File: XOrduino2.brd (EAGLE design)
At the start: 94 x 54.1 mm, 82 parts, among them J1 2.5mm, J2 2.5mm, J3 2.5mm, J4 2.5mm, J5 Batt In, J6 MOT R, J7 MOT L, P1 10k, Q1 ALS-PT204-6C/L177, SW1 RESET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

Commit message: v5 gerbers.
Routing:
- net GND: track 397.7 -> 416.2 mm, vias 6 -> 10
- net RD_P: track 26.5 -> 33.7 mm
- net +5V: track 226.1 -> 228.0 mm, vias 5 -> 7
- net XUSB: track 42.7 -> 44.4 mm
- net AREF: track 80.0 -> 81.5 mm
- net A2: track 44.5 -> 45.8 mm
- net A0: track 65.3 -> 64.3 mm
- net A1: track 57.2 -> 56.4 mm
- net N$8: track 99.0 -> 98.2 mm
- net MISO: track 30.2 -> 31.0 mm
- net N$11: track 26.1 -> 26.8 mm
- net VUSB: track 44.5 -> 43.9 mm
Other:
- board size 94 x 54.1 mm -> 81.3 x 53.3 mm
- board text added: "Alt Routing for LIGHT/A5"

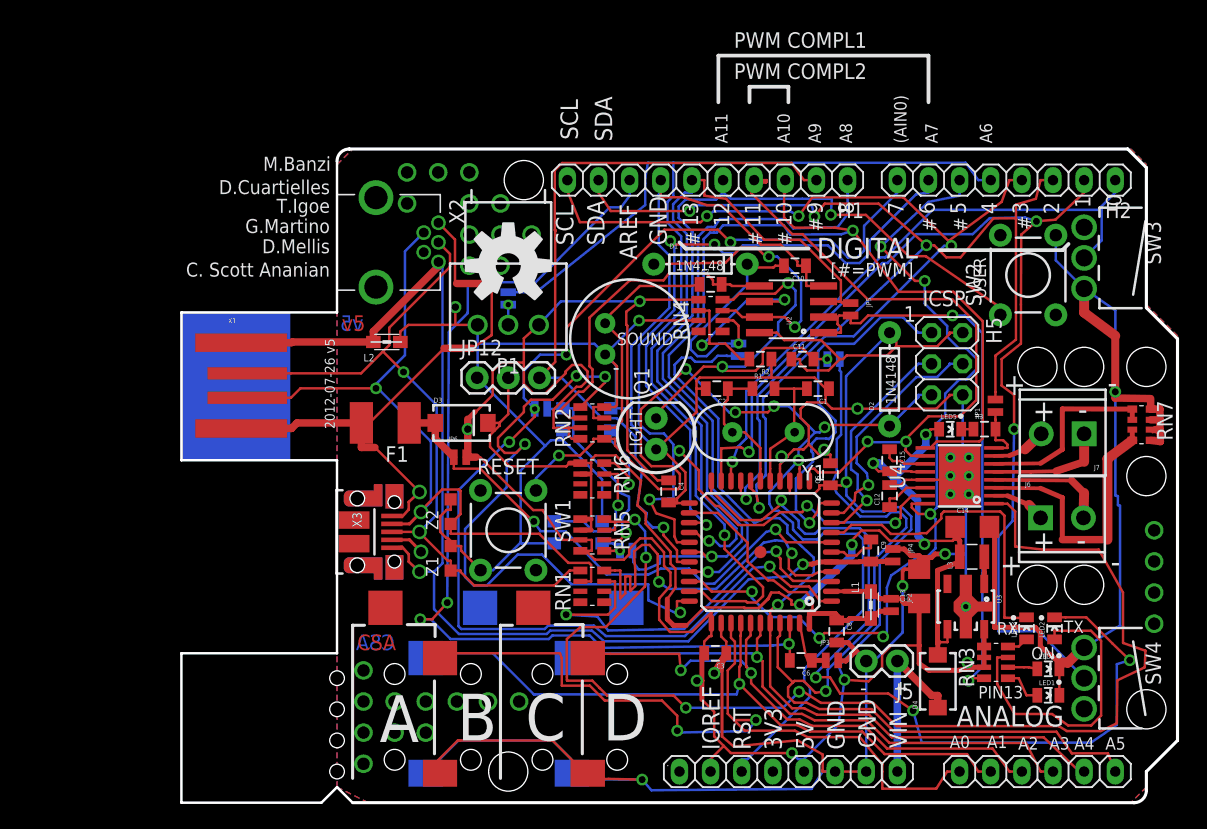
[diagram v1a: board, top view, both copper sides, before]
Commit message: Attempt 2 at routing the XOrduino2 board, via 10mil traces & spaces this time.
...however, the router still doesn't have quite the right via clearances.
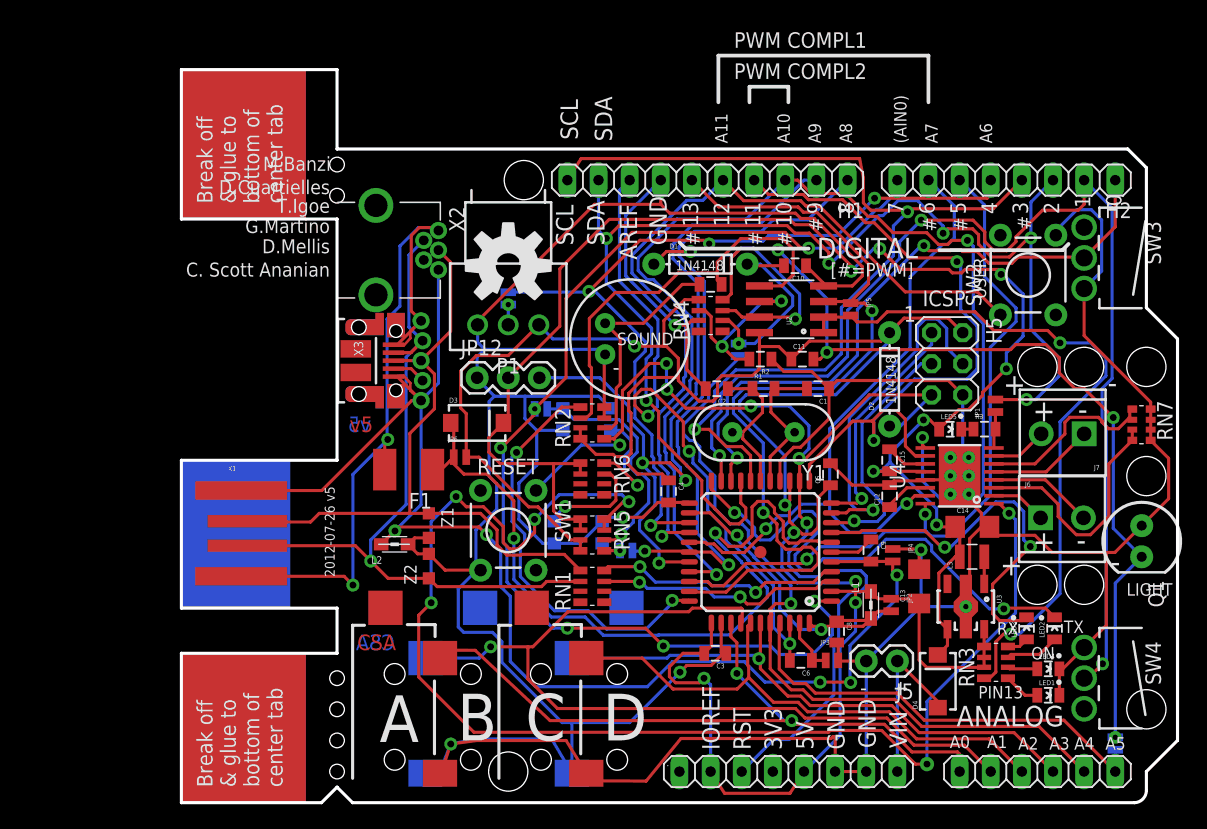
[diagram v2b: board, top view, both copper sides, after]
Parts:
- moved Q1 40.6 mm to (78.4, 21.3), turned to 270 degrees
- moved JP8 38.9 mm to (76.2, 4.83), turned to 270 degrees
- moved L2 16.5 mm to (17.4, 21.1)
- moved X3 14.0 mm to (14.5, 36.1)
- moved X1 12.1 mm to (5.08, 22.0)
- moved Z2 4.79 mm to (20.2, 19.3)
- moved F1 4.26 mm to (18.5, 27.2)
- moved Z1 3.21 mm to (20.2, 22.6), turned to 270 degrees
- moved D3 1.27 mm to (24.1, 31.0)
- moved X2 0.63 mm to (15.9, 45.1)
- moved J3 0.13 mm to (29.3, 0.00)
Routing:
- net LIGHT: track 34.3 -> 74.1 mm, vias 2 -> 3
- net A5: track 74.5 -> 36.4 mm, vias 1 -> 0
- net TXLED: track 72.8 -> 42.5 mm, vias 4 -> 2
- net D6*: track 84.7 -> 55.7 mm, vias 6 -> 2
- net AREF: track 81.5 -> 53.8 mm
- net VUSB: track 43.9 -> 64.4 mm
- net UGND: track 90.7 -> 111.0 mm, vias 1 -> 5
- net N$4: track 24.5 -> 4.41 mm
- net HWB: track 54.4 -> 34.3 mm, vias 4 -> 2
- net VCCIO: track 105.0 -> 124.3 mm, vias 5 -> 7
- net +5V: track 228.0 -> 210.0 mm, vias 7 -> 6
- net A1: track 56.4 -> 72.3 mm
- net XUSB: track 44.4 -> 58.1 mm, vias 0 -> 2
- net RD_M: track 33.7 -> 20.1 mm
- net RD_P: track 33.7 -> 20.2 mm
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- removed copper zone on layer 15, net +5V
- removed copper zone on layer 16, net GND
- removed copper zone on layer 1, net VCCIO
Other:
- board size 81.3 x 53.3 mm -> 81.3 x 59.8 mm
- board text added: "& glue to"
- board text added: "Break off"
- board text added: "bottom of"
- board text added: "center tab"

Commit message: Xorduino v6: rerouting with bigger vias, 10 mil traces, and better spacing.
Also added silkscreen, etc. and regenerated PDFs.
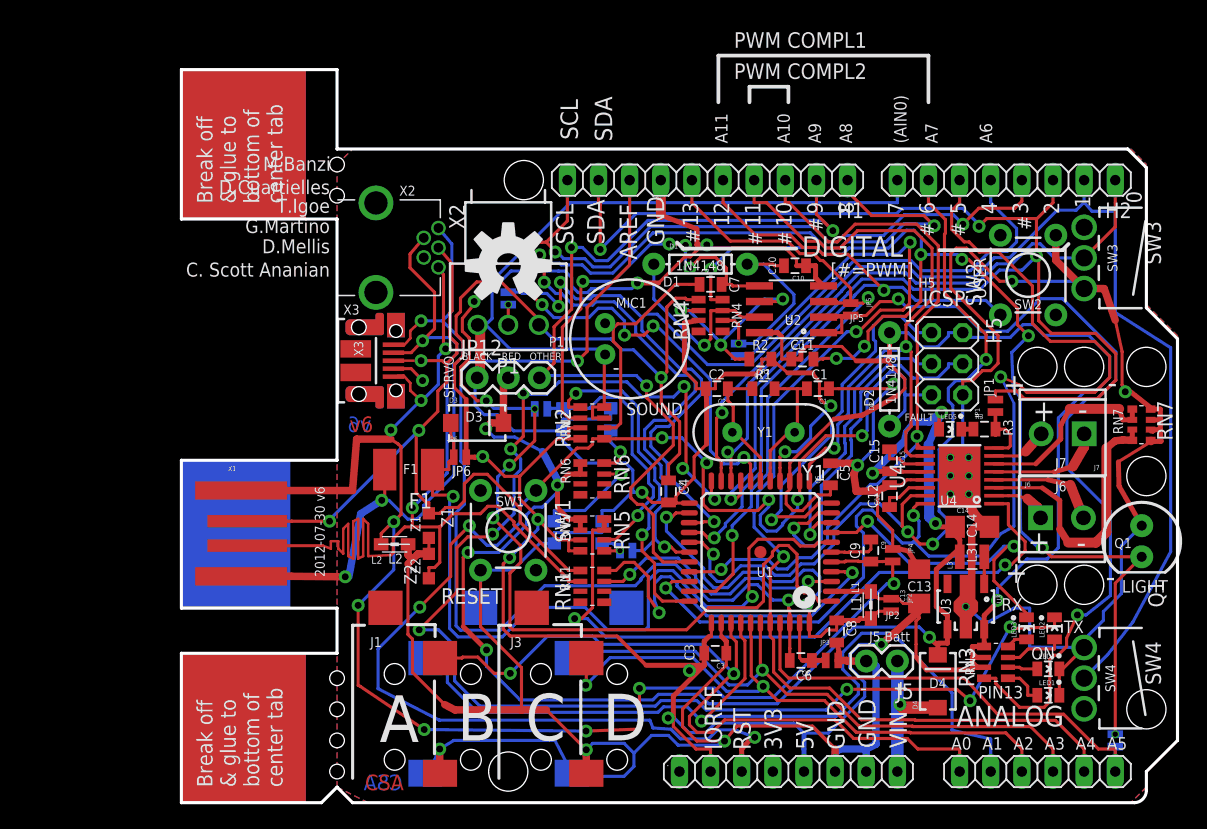
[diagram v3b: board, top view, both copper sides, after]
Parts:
- moved JP8 0.25 mm to (76.2, 5.08)
- moved X2 0.20 mm to (15.9, 45.3)
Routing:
- net TXLED: track 42.5 -> 113.2 mm, vias 2 -> 10
- net +5V: track 210.0 -> 264.9 mm, vias 6 -> 8
- net N$8: track 108.6 -> 55.9 mm, vias 6 -> 2
- net IO10*: track 96.6 -> 59.6 mm, vias 3 -> 2
- net D5*: track 58.9 -> 93.5 mm, vias 2 -> 3
- net IO8: track 53.8 -> 85.3 mm, vias 2 -> 4
- net AREF: track 53.8 -> 84.5 mm, vias 3 -> 2
- net A4: track 63.9 -> 91.2 mm, vias 1 -> 3
- net RESET: track 92.2 -> 117.8 mm, vias 6 -> 8
- net D_M: track 60.4 -> 85.3 mm
- net GND: track 408.5 -> 432.9 mm, vias 5 -> 12
- net LIGHT: track 74.1 -> 94.2 mm, vias 3 -> 7
- net D7: track 92.6 -> 109.4 mm, vias 5 -> 4
- net IO13*: track 70.8 -> 54.1 mm
- net N$6: track 57.8 -> 74.3 mm
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- added copper zone on layer 15, net +5V
- added copper zone on layer 16, net GND
- added copper zone on layer 1, net VCCIO
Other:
- board text added: "2012-07-30 v6"
- board text added: "BLACK"
- board text added: "Bottom"
- board text added: "C1"
- board text added: "C10"
- board text added: "C11"
- board text added: "C12"
- board text added: "C13"
- board text added: "C14"
- board text added: "C15"
- board text added: "C2"
- board text added: "C3"
- board text added: "C4"
- board text added: "C5"
- board text added: "C6"
- board text added: "C7"
- board text added: "C8"
- board text added: "C9"
- board text added: "Cut JP2 if populating L1"
- board text added: "Cut JP5 if populating U2"
- board text added: "Cut JP6 if populating U3"
- board text added: "D1"
- board text added: "D2"
- board text added: "D3"
- board text added: "D4"
- board text added: "F1"
- board text added: "FAULT"
- board text added: "H5"
- board text added: "J1"
- board text added: "J2"
- board text added: "J3"
- board text added: "J4"
- board text added: "J5 Batt"
- board text added: "J6"
- board text added: "J7"
- board text added: "JP1"
- board text added: "JP10"
- board text added: "JP11"
- board text added: "JP2"
- board text added: "JP5"
- board text added: "JP6"
- board text added: "JP7"
- board text added: "JP8"
- board text added: "JP9"
- board text added: "L1"
- board text added: "L2"
- board text added: "L3"
- board text added: "MIC1"
- board text added: "OLPC-F"
- board text added: "OTHER"
- board text added: "P1"
- board text added: "Q1"
- board text added: "R1"
- board text added: "R2"
- board text added: "R3"
- board text added: "RED"
- board text added: "RN1"
- board text added: "RN2"
- board text added: "RN3"
- board text added: "RN4"
- board text added: "RN5"
- board text added: "RN6"
- board text added: "RN7"
- board text added: "SERVO"
- board text added: "SW1"
- board text added: "SW2"
- board text added: "SW3"
- board text added: "SW4"
- board text added: "U1"
- board text added: "U2"
- board text added: "U3"
- board text added: "U4"
- board text added: "U5"
- board text added: "U6"
- board text added: "X2"
- board text added: "X3"
- board text added: "Y1"
- board text added: "Z1"
- board text added: "Z2"
- board text added: "v6"
- board text removed: "2012-07-26 v5"
- board text removed: "v5"

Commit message: v7: Update USB mini-B footprint & bom; more heat sink area for motor driver.
Went through and widened power traces as much as I could, as well.
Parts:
- JP9: device xorduino:SJ-2S-BOT-TRACE-VIA-NOCONFLICT -> xorduino:SJ-2S-BOT-TRACE-NOCONFLICT
- moved Q1 0.25 mm to (78.1, 21.3)
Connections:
- net SLIDER: no longer JP9.VIA6
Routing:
- net D5*: track 93.5 -> 109.9 mm
- net GND: track 432.9 -> 440.1 mm
- net LIGHT: track 94.2 -> 100.3 mm
- net +5V: track 264.9 -> 268.6 mm, vias 8 -> 9
- net N$6: track 74.3 -> 70.8 mm
- net UGND: track 115.7 -> 118.7 mm
- net D_M: track 85.3 -> 88.2 mm
- net RXLED: track 25.2 -> 27.6 mm
- net XUSB: track 50.6 -> 53.0 mm
- net VCCIO: track 122.7 -> 125.0 mm
- net D_P: track 62.3 -> 64.5 mm
- net D6*: track 67.3 -> 69.4 mm
- net N$8: track 55.9 -> 57.4 mm
- net A1: track 74.0 -> 75.4 mm
- net D1/TX: vias 1 -> 3
- added copper zone on layer 1, net GND
- removed copper zone on layer 1, net VCCIO
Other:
- board text added: "2012-08-01 v7"
- board text added: "v7"
- board text removed: "2012-07-30 v6"
- board text removed: "v6"
